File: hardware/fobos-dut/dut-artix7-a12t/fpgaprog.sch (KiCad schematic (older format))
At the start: 28 parts

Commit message: started adding FPGA to Artix7 DUT
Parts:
- removed C? (x3): 100nF, Capacitor_SMD:C_0603_1608Metric, symbol Device:C
- removed J?: Target, Connector_IDC:IDC-Header_2x10_P2.54mm_Horizontal, symbol Connector_Generic:Conn_02x10_Odd_Even
- removed J?: Pmod 2x6, symbol Connector_Generic:Conn_02x06_Top_Bottom
- removed R? (x12): 22R, Resistor_SMD:R_0603_1608Metric, symbol Device:R
- removed R? (x8): 200R, Resistor_SMD:R_0603_1608Metric, symbol Device:R
- removed U? (x3): SP3003-04ATG, Package_SO:MSOP-10_3x3mm_P0.5mm, symbol cerg:SP3003-04ATG
- added J?: JTAG, symbol Connector_Generic:Conn_02x07_Odd_Even
- added R? (x3): 4k7, Resistor_SMD:R_0603_1608Metric, symbol Device:R
- added SW?: MODE, symbol Switch:SW_DIP_x03
- added U1: XC7A12T-CSG325, Package_BGA:Xilinx_CSG325, symbol cerg:XC7A12T-CSG325
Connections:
- net labels added: FPGA_CCLK, VCCIO
- net labels removed: +3V3, Aux, CLK_C2D, CLK_D2C, CV_RST, CW_HS1, CW_HS2, CW_MISO, CW_MOSI, CW_PDIC, CW_PDID, CW_SCK, CW_TARG1, CW_TARG2, CW_TARG3, CW_TARG4, CW_VREF, DIO0, DIO1, DIO2, DIO3, FS_3V3, FS_5V, IO, JA1, JA10, JA2, JA3, JA4, JA7, JA8, JA9, RST, Ready, TF, Valid
- wire segments 139 -> 48
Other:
- note removed: "ESD Protection"
- note removed: "FOBOS Target Connector"
- note removed: "PMOD Connector"

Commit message: artix 7 dut updates
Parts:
- gave numbers to parts that had none: 5
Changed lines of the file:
@@
 $EndBitmap
 $Comp
-L Switch:SW_DIP_x03 SW?
+L Switch:SW_DIP_x03 SW1
 U 1 1 5F5037BE
 P 4500 3200
-F 0 "SW?" H 4500 3667 50  0000 C CNN
+F 0 "SW1" H 4500 3667 50  0000 C CNN
 F 1 "MODE" H 4500 3576 50  0000 C CNN
 F 2 "" H 4500 3200 50  0001 C CNN
@@
 $EndComp
 $Comp
-L power:GND #PWR?
+L power:GND #PWR0129
 U 1 1 5F505FAD
 P 4100 3300
-F 0 "#PWR?" H 4100 3050 50  0001 C CNN
+F 0 "#PWR0129" H 4100 3050 50  0001 C CNN
 F 1 "GND" H 4105 3127 50  0000 C CNN
 F 2 "" H 4100 3300 50  0001 C CNN
@@
 	4800 3200 5350 3200
 $Comp
-L Device:R R?
+L Device:R R33
 U 1 1 5F5112B7
 P 5350 2100
-F 0 "R?" V 5450 1950 50  0000 L CNN
+F 0 "R33" V 5450 1950 50  0000 L CNN
 F 1 "4k7" V 5450 2100 50  0000 L CNN
 F 2 "Resistor_SMD:R_0603_1608Metric" V 5280 2100 50  0001 C CNN
@@
 $EndComp
 $Comp
-L Device:R R?
+L Device:R R32
 U 1 1 5F518AC2
 P 5150 2100
-F 0 "R?" V 5250 1950 50  0000 L CNN
+F 0 "R32" V 5250 1950 50  0000 L CNN
 F 1 "4k7" V 5250 2100 50  0000 L CNN
 F 2 "Resistor_SMD:R_0603_1608Metric" V 5080 2100 50  0001 C CNN
@@
 $EndComp
 $Comp
-L Device:R R?
+L Device:R R31
 U 1 1 5F518EEF
 P 4950 2100
-F 0 "R?" V 5050 1950 50  0000 L CNN
+F 0 "R31" V 5050 1950 50  0000 L CNN
 F 1 "4k7" V 5050 2100 50  0000 L CNN
 F 2 "Resistor_SMD:R_0603_1608Metric" V 4880 2100 50  0001 C CNN
@@
 Connection ~ 5150 1850
 $Comp
-L cerg:VCCIO #PWR?
+L cerg:VCCIO #PWR0130
 U 1 1 5F520C1F
 P 5150 1750
-F 0 "#PWR?" H 5150 1600 50  0001 C CNN
+F 0 "#PWR0130" H 5150 1600 50  0001 C CNN
 F 1 "VCCIO" V 5050 1850 50  0000 C CNN
 F 2 "" H 5150 1750 50  0001 C CNN
@@
 	5150 1750 5150 1850
 $Comp
-L Connector_Generic:Conn_02x07_Odd_Even J?
+L Connector_Generic:Conn_02x07_Odd_Even J7
 U 1 1 5F5293C6
 P 4850 3900
-F 0 "J?" H 4900 4417 50  0000 C CNN
+F 0 "J7" H 4900 4417 50  0000 C CNN
 F 1 "JTAG" H 4900 4326 50  0000 C CNN
 F 2 "" H 4850 3900 50  0001 C CNN
@@
 $EndComp
 $Comp
-L power:GND #PWR?
+L power:GND #PWR0131
 U 1 1 5F52AC29
 P 4550 4350
-F 0 "#PWR?" H 4550 4100 50  0001 C CNN
+F 0 "#PWR0131" H 4550 4100 50  0001 C CNN
 F 1 "GND" H 4555 4177 50  0000 C CNN
 F 2 "" H 4550 4350 50  0001 C CNN
@@
 Connection ~ 4550 3700
 $Comp
-L cerg:VCCIO #PWR?
+L cerg:VCCIO #PWR0132
 U 1 1 5F5300B6
 P 5250 3550
-F 0 "#PWR?" H 5250 3400 50  0001 C CNN
+F 0 "#PWR0132" H 5250 3400 50  0001 C CNN
 F 1 "VCCIO" H 5262 3807 50  0000 C CNN
 F 2 "" H 5250 3550 50  0001 C CNN

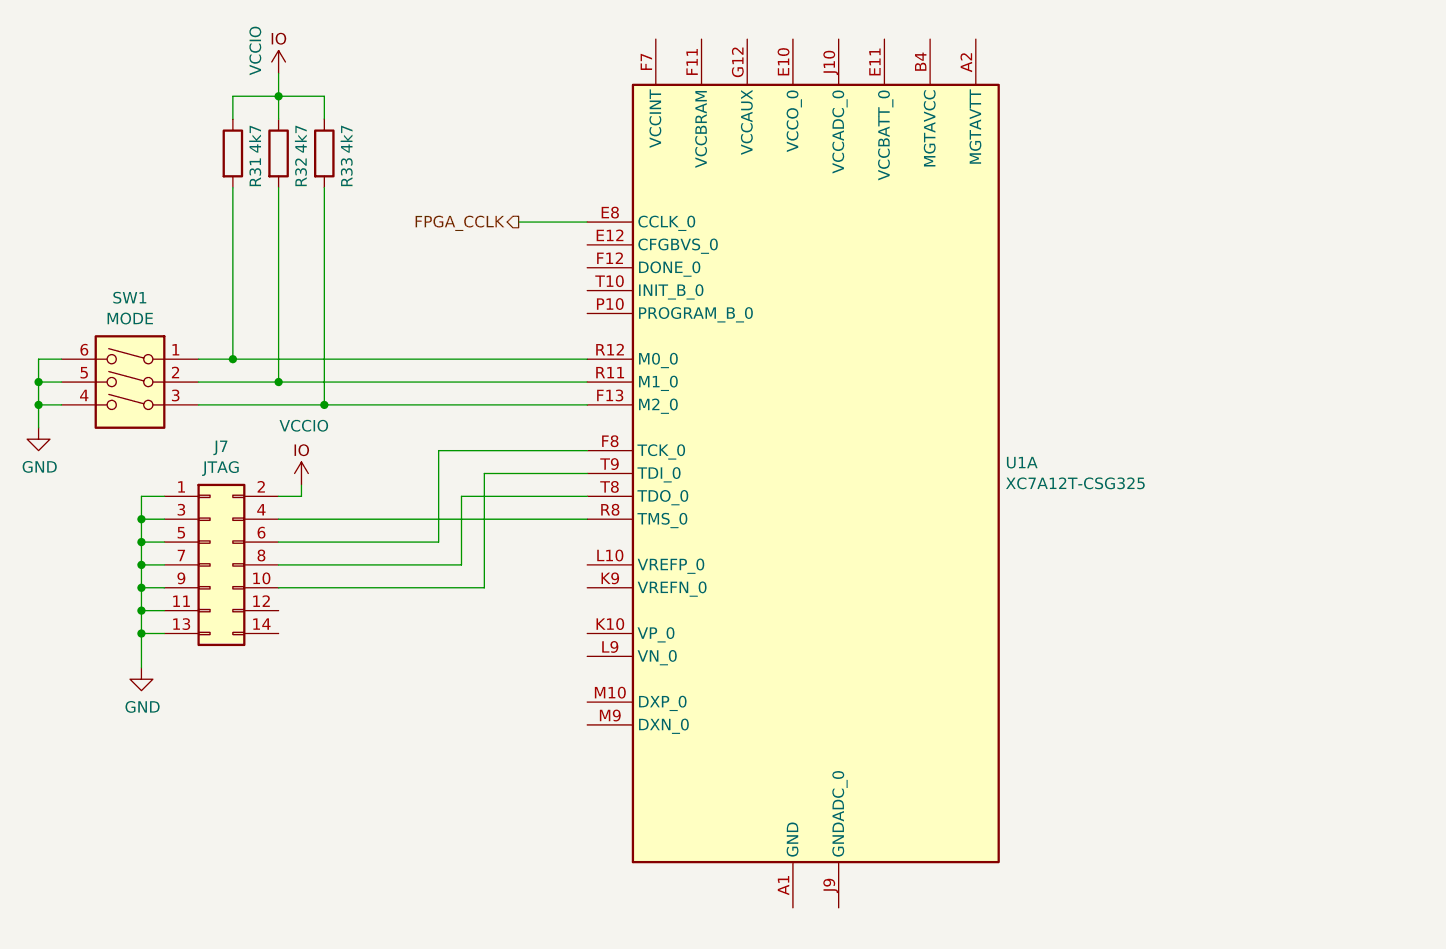
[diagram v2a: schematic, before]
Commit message: Added LTC3633 power regulator to serve as the main system power supply
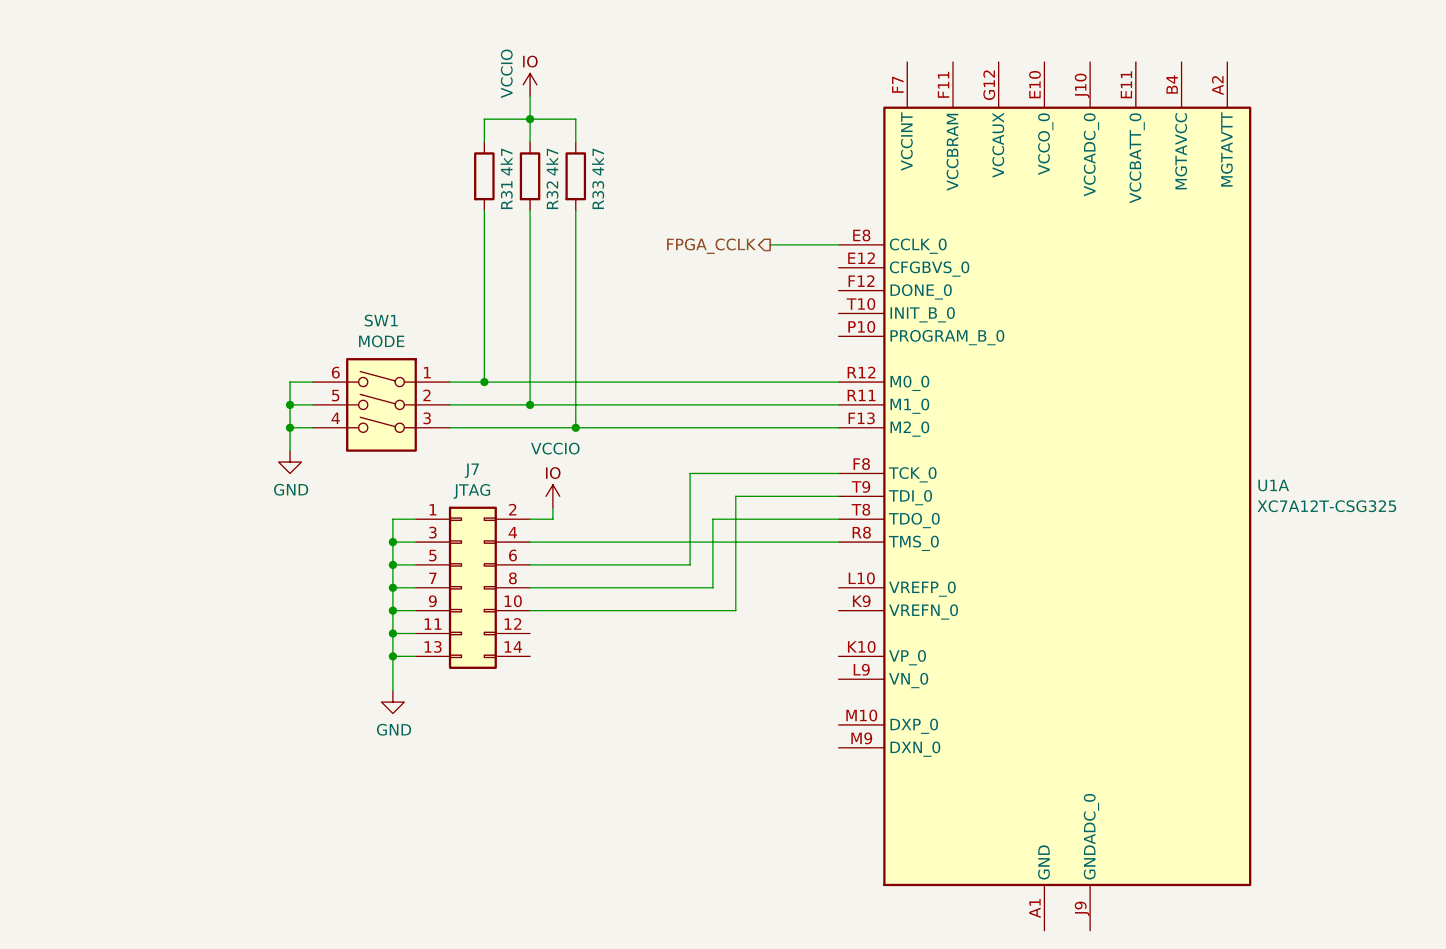
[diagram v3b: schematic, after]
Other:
- moved on the sheet: J7, R31, R32, R33, SW1, U1A

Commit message: -Added TS3A27518EIPWRQ1 6 circuit analog SPDT switch -Connected tripple output power supply to FPGA power pins -Added bypass and decoupling capacitors to the FPGA power pins(these will be DNP) -Swapped out the old bulky banana jack socket parts for 1050752001 and 1050753001 -Added JTAG header -Added test loops -Added boot mode dip switch -Swapped out the right angle 0.1" headers for vertical 0.1" headers(personal preference) -Working my way through the 7_series_schematic_review_recommendations spreadsheet
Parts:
- removed J7: JTAG, symbol Connector_Generic:Conn_02x07_Odd_Even
- removed SW1: MODE, symbol Switch:SW_DIP_x03
- added C25: 100uF, Resistor_SMD:R_1210_3225Metric_Pad1.30x2.65mm_HandSolder, symbol Device:C
- added C26, C27, C35: 47uF, Resistor_SMD:R_1210_3225Metric_Pad1.30x2.65mm_HandSolder, symbol Device:C
- added C28, C29, C36, C37, C38, C39, C40, C41: 4.7uF, Resistor_SMD:R_0805_2012Metric_Pad1.20x1.40mm_HandSolder, symbol Device:C
- added C30, C31, C32, C33, C34, C42, C43, C44, C45, C46, C47, C48, C49, C50, C51, C52, C53: .47uF, Resistor_SMD:R_0603_1608Metric_Pad0.98x0.95mm_HandSolder, symbol Device:C
- added J7: 0878321420, digikey-footprints:PinHeader_2x7_P2mm_SMD, symbol dk_Rectangular-Connectors-Headers-Male-Pins:0878321420
- added SW1: SW_DIP_x03, cerg:DS04-254-2-03BK-SMT, symbol cerg:SW_DIP_x03
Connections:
- net labels added: +1V0, +1V8, +3V3, VCCAUX, VCCINT
- wire segments 48 -> 201
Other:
- note added: "BANK0\nE10, R10"
- note added: "BANK14\nL16, P17, R14, T11, U8, U18, V15"
- note added: "BANK15\nA16, B13, C10, D17, E14, G18, H15"
- note added: "BANK34\nL6, M3, P7, R4, T1, V5"
- moved on the sheet: R31, R32, R33, U1A

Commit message: Schematic is 99% complete, getting started on layout
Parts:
- added R29: 0R, Resistor_SMD:R_0603_1608Metric, symbol Device:R
- added R53: 330R, Resistor_SMD:R_0603_1608Metric, symbol Device:R
- added R54, R55: 4.7KR, Resistor_SMD:R_0603_1608Metric, symbol Device:R
- added S2: 1825910-6, digikey-footprints:Switch_Tactile_THT_6x6mm, symbol dk_Tactile-Switches:1825910-6
- R31, R32, R33: value 4k7 -> 4.7KR
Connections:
- net labels added: SW_CLK, SW_DONE, SW_INIT_B, SW_PROGRAM_B
- net labels removed: +1V0, FPGA_CCLK, VCCAUX, VCCIO
- wire segments 201 -> 213
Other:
- note added: "Verify 330R\n"
- moved on the sheet: C27

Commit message: Preliminary placement underway Made a copy of cerg 3d model within Artix 7 dut project to resolve nagging library path issue
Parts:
- C26, C27, C35: footprint Resistor_SMD:R_1210_3225Metric_Pad1.30x2.65mm_HandSolder -> Resistor_SMD:R_0805_2012Metric_Pad1.20x1.40mm_HandSolder
- C28, C29, C36, C37, C38, C39, C40, C41: footprint Resistor_SMD:R_0805_2012Metric_Pad1.20x1.40mm_HandSolder -> Resistor_SMD:R_0402_1005Metric_Pad0.72x0.64mm_HandSolder
- C30, C31, C32, C33, C34, C42, C43, C44, C45, C46, C47, C48, C49, C50, C51, C52, C53: footprint Resistor_SMD:R_0603_1608Metric_Pad0.98x0.95mm_HandSolder -> Resistor_SMD:R_0402_1005Metric_Pad0.72x0.64mm_HandSolder
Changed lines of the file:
@@
 F 0 "C29" H 1915 2196 50  0000 L CNN
 F 1 "4.7uF" H 1915 2105 50  0000 L CNN
-F 2 "Resistor_SMD:R_0805_2012Metric_Pad1.20x1.40mm_HandSolder" H 1838 2000 50  0001 C CNN
+F 2 "Resistor_SMD:R_0402_1005Metric_Pad0.72x0.64mm_HandSolder" H 1838 2000 50  0001 C CNN
 F 3 "~" H 1800 2150 50  0001 C CNN
 	1    1800 2150
@@
 F 0 "C30" H 2415 2196 50  0000 L CNN
 F 1 ".47uF" H 2415 2105 50  0000 L CNN
-F 2 "Resistor_SMD:R_0603_1608Metric_Pad0.98x0.95mm_HandSolder" H 2338 2000 50  0001 C CNN
+F 2 "Resistor_SMD:R_0402_1005Metric_Pad0.72x0.64mm_HandSolder" H 2338 2000 50  0001 C CNN
 F 3 "~" H 2300 2150 50  0001 C CNN
 	1    2300 2150
@@
 F 0 "C32" H 2915 2196 50  0000 L CNN
 F 1 ".47uF" H 2915 2105 50  0000 L CNN
-F 2 "Resistor_SMD:R_0603_1608Metric_Pad0.98x0.95mm_HandSolder" H 2838 2000 50  0001 C CNN
+F 2 "Resistor_SMD:R_0402_1005Metric_Pad0.72x0.64mm_HandSolder" H 2838 2000 50  0001 C CNN
 F 3 "~" H 2800 2150 50  0001 C CNN
 	1    2800 2150
@@
 F 0 "C26" H 1415 3446 50  0000 L CNN
 F 1 "47uF" H 1415 3355 50  0000 L CNN
-F 2 "Resistor_SMD:R_1210_3225Metric_Pad1.30x2.65mm_HandSolder" H 1338 3250 50  0001 C CNN
+F 2 "Resistor_SMD:R_0805_2012Metric_Pad1.20x1.40mm_HandSolder" H 1338 3250 50  0001 C CNN
 F 3 "~" H 1300 3400 50  0001 C CNN
 	1    1300 3400
@@
 F 0 "C28" H 1865 3446 50  0000 L CNN
 F 1 "4.7uF" H 1865 3355 50  0000 L CNN
-F 2 "Resistor_SMD:R_0805_2012Metric_Pad1.20x1.40mm_HandSolder" H 1788 3250 50  0001 C CNN
+F 2 "Resistor_SMD:R_0402_1005Metric_Pad0.72x0.64mm_HandSolder" H 1788 3250 50  0001 C CNN
 F 3 "~" H 1750 3400 50  0001 C CNN
 	1    1750 3400
@@
 F 0 "C31" H 2415 3446 50  0000 L CNN
 F 1 ".47uF" H 2415 3355 50  0000 L CNN
-F 2 "Resistor_SMD:R_0603_1608Metric_Pad0.98x0.95mm_HandSolder" H 2338 3250 50  0001 C CNN
+F 2 "Resistor_SMD:R_0402_1005Metric_Pad0.72x0.64mm_HandSolder" H 2338 3250 50  0001 C CNN
 F 3 "~" H 2300 3400 50  0001 C CNN
 	1    2300 3400
@@
 F 0 "C33" H 2915 3446 50  0000 L CNN
 F 1 ".47uF" H 2915 3355 50  0000 L CNN
-F 2 "Resistor_SMD:R_0603_1608Metric_Pad0.98x0.95mm_HandSolder" H 2838 3250 50  0001 C CNN
+F 2 "Resistor_SMD:R_0402_1005Metric_Pad0.72x0.64mm_HandSolder" H 2838 3250 50  0001 C CNN
 F 3 "~" H 2800 3400 50  0001 C CNN
 	1    2800 3400
@@
 F 0 "C27" H 3515 3446 50  0000 L CNN
 F 1 "47uF" H 3515 3355 50  0000 L CNN
-F 2 "Resistor_SMD:R_1210_3225Metric_Pad1.30x2.65mm_HandSolder" H 3438 3250 50  0001 C CNN
+F 2 "Resistor_SMD:R_0805_2012Metric_Pad1.20x1.40mm_HandSolder" H 3438 3250 50  0001 C CNN
 F 3 "~" H 3400 3400 50  0001 C CNN
 	1    3400 3400
@@
 F 0 "C35" H 4065 2196 50  0000 L CNN
 F 1 "47uF" H 4065 2105 50  0000 L CNN
-F 2 "Resistor_SMD:R_1210_3225Metric_Pad1.30x2.65mm_HandSolder" H 3988 2000 50  0001 C CNN
+F 2 "Resistor_SMD:R_0805_2012Metric_Pad1.20x1.40mm_HandSolder" H 3988 2000 50  0001 C CNN
 F 3 "~" H 3950 2150 50  0001 C CNN
 	1    3950 2150
@@
 F 0 "C34" H 3465 2196 50  0000 L CNN
 F 1 ".47uF" H 3465 2105 50  0000 L CNN
-F 2 "Resistor_SMD:R_0603_1608Metric_Pad0.98x0.95mm_HandSolder" H 3388 2000 50  0001 C CNN
+F 2 "Resistor_SMD:R_0402_1005Metric_Pad0.72x0.64mm_HandSolder" H 3388 2000 50  0001 C CNN
 F 3 "~" H 3350 2150 50  0001 C CNN
 	1    3350 2150
@@
 F 0 "C36" H 1415 4596 50  0000 L CNN
 F 1 "4.7uF" H 1415 4505 50  0000 L CNN
-F 2 "Resistor_SMD:R_0805_2012Metric_Pad1.20x1.40mm_HandSolder" H 1338 4400 50  0001 C CNN
+F 2 "Resistor_SMD:R_0402_1005Metric_Pad0.72x0.64mm_HandSolder" H 1338 4400 50  0001 C CNN
 F 3 "~" H 1300 4550 50  0001 C CNN
 	1    1300 4550
@@
 F 0 "C39" H 1865 4596 50  0000 L CNN
 F 1 "4.7uF" H 1865 4505 50  0000 L CNN
-F 2 "Resistor_SMD:R_0805_2012Metric_Pad1.20x1.40mm_HandSolder" H 1788 4400 50  0001 C CNN
+F 2 "Resistor_SMD:R_0402_1005Metric_Pad0.72x0.64mm_HandSolder" H 1788 4400 50  0001 C CNN
 F 3 "~" H 1750 4550 50  0001 C CNN
 	1    1750 4550
@@
 F 0 "C42" H 2415 4596 50  0000 L CNN
 F 1 ".47uF" H 2415 4505 50  0000 L CNN
-F 2 "Resistor_SMD:R_0603_1608Metric_Pad0.98x0.95mm_HandSolder" H 2338 4400 50  0001 C CNN
+F 2 "Resistor_SMD:R_0402_1005Metric_Pad0.72x0.64mm_HandSolder" H 2338 4400 50  0001 C CNN
 F 3 "~" H 2300 4550 50  0001 C CNN
 	1    2300 4550
@@
 F 0 "C47" H 2915 4596 50  0000 L CNN
 F 1 ".47uF" H 2915 4505 50  0000 L CNN
-F 2 "Resistor_SMD:R_0603_1608Metric_Pad0.98x0.95mm_HandSolder" H 2838 4400 50  0001 C CNN
+F 2 "Resistor_SMD:R_0402_1005Metric_Pad0.72x0.64mm_HandSolder" H 2838 4400 50  0001 C CNN
 F 3 "~" H 2800 4550 50  0001 C CNN
 	1    2800 4550
@@
 F 0 "C37" H 1415 5796 50  0000 L CNN
 F 1 "4.7uF" H 1415 5705 50  0000 L CNN
-F 2 "Resistor_SMD:R_0805_2012Metric_Pad1.20x1.40mm_HandSolder" H 1338 5600 50  0001 C CNN
+F 2 "Resistor_SMD:R_0402_1005Metric_Pad0.72x0.64mm_HandSolder" H 1338 5600 50  0001 C CNN
 F 3 "~" H 1300 5750 50  0001 C CNN
 	1    1300 5750
@@
 F 0 "C40" H 1865 5796 50  0000 L CNN
 F 1 "4.7uF" H 1865 5705 50  0000 L CNN
-F 2 "Resistor_SMD:R_0805_2012Metric_Pad1.20x1.40mm_HandSolder" H 1788 5600 50  0001 C CNN
+F 2 "Resistor_SMD:R_0402_1005Metric_Pad0.72x0.64mm_HandSolder" H 1788 5600 50  0001 C CNN
 F 3 "~" H 1750 5750 50  0001 C CNN
 	1    1750 5750
@@
 F 0 "C43" H 2415 5796 50  0000 L CNN
 F 1 ".47uF" H 2415 5705 50  0000 L CNN
-F 2 "Resistor_SMD:R_0603_1608Metric_Pad0.98x0.95mm_HandSolder" H 2338 5600 50  0001 C CNN
+F 2 "Resistor_SMD:R_0402_1005Metric_Pad0.72x0.64mm_HandSolder" H 2338 5600 50  0001 C CNN
 F 3 "~" H 2300 5750 50  0001 C CNN
 	1    2300 5750
@@
 F 0 "C45" H 2865 5796 50  0000 L CNN
 F 1 ".47uF" H 2865 5705 50  0000 L CNN
-F 2 "Resistor_SMD:R_0603_1608Metric_Pad0.98x0.95mm_HandSolder" H 2788 5600 50  0001 C CNN
+F 2 "Resistor_SMD:R_0402_1005Metric_Pad0.72x0.64mm_HandSolder" H 2788 5600 50  0001 C CNN
 F 3 "~" H 2750 5750 50  0001 C CNN
 	1    2750 5750
@@
 F 0 "C48" H 3415 4596 50  0000 L CNN
 F 1 ".47uF" H 3415 4505 50  0000 L CNN
-F 2 "Resistor_SMD:R_0603_1608Metric_Pad0.98x0.95mm_HandSolder" H 3338 4400 50  0001 C CNN
+F 2 "Resistor_SMD:R_0402_1005Metric_Pad0.72x0.64mm_HandSolder" H 3338 4400 50  0001 C CNN
 F 3 "~" H 3300 4550 50  0001 C CNN
 	1    3300 4550
@@
 F 0 "C51" H 3965 4596 50  0000 L CNN
 F 1 ".47uF" H 3965 4505 50  0000 L CNN
-F 2 "Resistor_SMD:R_0603_1608Metric_Pad0.98x0.95mm_HandSolder" H 3888 4400 50  0001 C CNN
+F 2 "Resistor_SMD:R_0402_1005Metric_Pad0.72x0.64mm_HandSolder" H 3888 4400 50  0001 C CNN
 F 3 "~" H 3850 4550 50  0001 C CNN
 	1    3850 4550
@@
 F 0 "C49" H 3415 5796 50  0000 L CNN
 F 1 ".47uF" H 3415 5705 50  0000 L CNN
-F 2 "Resistor_SMD:R_0603_1608Metric_Pad0.98x0.95mm_HandSolder" H 3338 5600 50  0001 C CNN
+F 2 "Resistor_SMD:R_0402_1005Metric_Pad0.72x0.64mm_HandSolder" H 3338 5600 50  0001 C CNN
 F 3 "~" H 3300 5750 50  0001 C CNN
 	1    3300 5750
@@
 F 0 "C52" H 3965 5796 50  0000 L CNN
 F 1 ".47uF" H 3965 5705 50  0000 L CNN
-F 2 "Resistor_SMD:R_0603_1608Metric_Pad0.98x0.95mm_HandSolder" H 3888 5600 50  0001 C CNN
+F 2 "Resistor_SMD:R_0402_1005Metric_Pad0.72x0.64mm_HandSolder" H 3888 5600 50  0001 C CNN
 F 3 "~" H 3850 5750 50  0001 C CNN
 	1    3850 5750
@@
 F 0 "C38" H 1415 7046 50  0000 L CNN
 F 1 "4.7uF" H 1415 6955 50  0000 L CNN
-F 2 "Resistor_SMD:R_0805_2012Metric_Pad1.20x1.40mm_HandSolder" H 1338 6850 50  0001 C CNN
+F 2 "Resistor_SMD:R_0402_1005Metric_Pad0.72x0.64mm_HandSolder" H 1338 6850 50  0001 C CNN
 F 3 "~" H 1300 7000 50  0001 C CNN
 	1    1300 7000
@@
 F 0 "C41" H 1865 7046 50  0000 L CNN
 F 1 "4.7uF" H 1865 6955 50  0000 L CNN
-F 2 "Resistor_SMD:R_0805_2012Metric_Pad1.20x1.40mm_HandSolder" H 1788 6850 50  0001 C CNN
+F 2 "Resistor_SMD:R_0402_1005Metric_Pad0.72x0.64mm_HandSolder" H 1788 6850 50  0001 C CNN
 F 3 "~" H 1750 7000 50  0001 C CNN
 	1    1750 7000
@@
 F 0 "C44" H 2415 7046 50  0000 L CNN
 F 1 ".47uF" H 2415 6955 50  0000 L CNN
-F 2 "Resistor_SMD:R_0603_1608Metric_Pad0.98x0.95mm_HandSolder" H 2338 6850 50  0001 C CNN
+F 2 "Resistor_SMD:R_0402_1005Metric_Pad0.72x0.64mm_HandSolder" H 2338 6850 50  0001 C CNN
 F 3 "~" H 2300 7000 50  0001 C CNN
 	1    2300 7000
@@
 F 0 "C46" H 2865 7046 50  0000 L CNN
 F 1 ".47uF" H 2865 6955 50  0000 L CNN
-F 2 "Resistor_SMD:R_0603_1608Metric_Pad0.98x0.95mm_HandSolder" H 2788 6850 50  0001 C CNN
+F 2 "Resistor_SMD:R_0402_1005Metric_Pad0.72x0.64mm_HandSolder" H 2788 6850 50  0001 C CNN
 F 3 "~" H 2750 7000 50  0001 C CNN
 	1    2750 7000
@@
 F 0 "C50" H 3415 7046 50  0000 L CNN
 F 1 ".47uF" H 3415 6955 50  0000 L CNN
-F 2 "Resistor_SMD:R_0603_1608Metric_Pad0.98x0.95mm_HandSolder" H 3338 6850 50  0001 C CNN
+F 2 "Resistor_SMD:R_0402_1005Metric_Pad0.72x0.64mm_HandSolder" H 3338 6850 50  0001 C CNN
 F 3 "~" H 3300 7000 50  0001 C CNN
 	1    3300 7000
@@
 F 0 "C53" H 3965 7046 50  0000 L CNN
 F 1 ".47uF" H 3965 6955 50  0000 L CNN
-F 2 "Resistor_SMD:R_0603_1608Metric_Pad0.98x0.95mm_HandSolder" H 3888 6850 50  0001 C CNN
+F 2 "Resistor_SMD:R_0402_1005Metric_Pad0.72x0.64mm_HandSolder" H 3888 6850 50  0001 C CNN
 F 3 "~" H 3850 7000 50  0001 C CNN
 	1    3850 7000
